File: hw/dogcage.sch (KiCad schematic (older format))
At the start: 17 parts, among them CON1 BARREL_JACK, M1 XBEE, P1 Door Sensor, P2 Servo, P3 CONN_01X10, P4 CONN_01X10, P5 CONN_01X14, P7 CONN_01X14, Q1 TIP120, SW1 SW_PUSH, U1 LD1117S33TR, U2 TEENSYLC

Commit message: Bulk cap to 5V and current limiting resistor to TIP120 base
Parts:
- added C3: 100uF, symbol C
- added R2: 470, symbol R
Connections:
- wire segments 89 -> 92
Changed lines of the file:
@@
 L +5V #PWR012
 U 1 1 553C62D3
-P 2950 1000
-F 0 "#PWR012" H 2950 850 50  0001 C CNN
-F 1 "+5V" H 2950 1140 50  0000 C CNN
-F 2 "" H 2950 1000 60  0000 C CNN
-F 3 "" H 2950 1000 60  0000 C CNN
-	1    2950 1000
+P 2850 1000
+F 0 "#PWR012" H 2850 850 50  0001 C CNN
+F 1 "+5V" H 2850 1140 50  0000 C CNN
+F 2 "" H 2850 1000 60  0000 C CNN
+F 3 "" H 2850 1000 60  0000 C CNN
+	1    2850 1000
 	1    0    0    -1
 $EndComp
@@
 	3250 1550 3250 1600
 Wire Wire Line
-	3250 1600 4450 1600
+	2900 1600 4450 1600
 Connection ~ 3850 1600
 Wire Wire Line
@@
 	2050 1150 2350 1150
 Wire Wire Line
-	2950 1000 2950 1150
-Wire Wire Line
-	2950 1150 3450 1150
+	2850 1000 2850 1150
+Wire Wire Line
+	2850 1150 3450 1150
 Wire Wire Line
 	3250 1250 3250 1150
@@
 	7850 3500 6850 3500
 Wire Wire Line
-	6850 3500 6850 4750
+	6850 3500 6850 4150
 Wire Wire Line
 	6850 4750 7150 4750
@@
 Text Label 8650 1600 0    60   ~ 0
 XBEE_CTL
+$Comp
+L R R2
+U 1 1 558214B8
+P 6850 4300
+F 0 "R2" V 6930 4300 50  0000 C CNN
+F 1 "470" V 6850 4300 50  0000 C CNN
+F 2 "" V 6780 4300 30  0000 C CNN
+F 3 "" H 6850 4300 30  0000 C CNN
+	1    6850 4300
+	1    0    0    -1
+$EndComp
+Wire Wire Line
+	6850 4750 6850 4450
+$Comp
+L C C3
+U 1 1 55821ABF
+P 2900 1400
+F 0 "C3" H 2925 1500 50  0000 L CNN
+F 1 "100uF" H 2925 1300 50  0000 L CNN
+F 2 "" H 2938 1250 30  0000 C CNN
+F 3 "" H 2900 1400 60  0000 C CNN
+	1    2900 1400
+	1    0    0    -1
+$EndComp
+Wire Wire Line
+	2900 1150 2900 1250
+Connection ~ 2900 1150
+Connection ~ 3250 1600
+Wire Wire Line
+	2900 1550 2900 1600
 $EndSCHEMATC

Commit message: Added lock servo
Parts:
- added P?: Lock, Pin_Headers:Pin_Header_Straight_1x03, symbol CONN_01X03
- added Q?: TIP120, ~, symbol TIP120
- added R?: 470, symbol R
- P2: value Servo -> Door
- Q1: footprint Power_Integrations:TO-220 -> ~
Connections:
- wire segments 92 -> 118
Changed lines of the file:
@@
 P 7950 4050
 F 0 "P2" H 7950 4250 50  0000 C CNN
-F 1 "Servo" V 8050 4050 50  0000 C CNN
+F 1 "Door" V 8050 4050 50  0000 C CNN
 F 2 "Pin_Headers:Pin_Header_Straight_1x03" H 7950 4050 60  0001 C CNN
 F 3 "" H 7950 4050 60  0000 C CNN
@@
 F 0 "Q1" H 7600 4825 50  0000 L CNN
 F 1 "TIP120" H 7600 4750 50  0000 L CNN
-F 2 "Power_Integrations:TO-220" H 7600 4675 50  0000 L CIN
+F 2 "~" H 7600 4675 50  0000 L CIN
 F 3 "" H 7350 4750 50  0000 L CNN
 	1    7350 4750
@@
 	7450 4150 7750 4150
 Wire Wire Line
-	4250 1150 4800 1150
+	4250 1150 4450 1150
+Wire Wire Line
+	4450 1150 4800 1150
 Wire Wire Line
 	4800 1150 4800 1000
 Wire Wire Line
-	3850 1450 3850 1700
+	3850 1450 3850 1600
+Wire Wire Line
+	3850 1600 3850 1700
 Wire Wire Line
 	3250 1550 3250 1600
 Wire Wire Line
-	2900 1600 4450 1600
+	2900 1600 3250 1600
+Wire Wire Line
+	3250 1600 3850 1600
+Wire Wire Line
+	3850 1600 4450 1600
 Connection ~ 3850 1600
 Wire Wire Line
@@
 	2850 1000 2850 1150
 Wire Wire Line
-	2850 1150 3450 1150
+	2850 1150 2900 1150
+Wire Wire Line
+	2900 1150 3250 1150
+Wire Wire Line
+	3250 1150 3450 1150
 Wire Wire Line
 	3250 1250 3250 1150
@@
 $EndComp
 Wire Wire Line
-	1500 2950 1950 2950
+	1500 2950 1750 2950
+Wire Wire Line
+	1750 2950 1950 2950
 Wire Wire Line
 	1500 3050 1950 3050
@@
 $EndComp
 Wire Wire Line
-	3750 3450 4300 3450
+	3750 3450 4000 3450
+Wire Wire Line
+	4000 3450 4300 3450
 Wire Wire Line
 	4000 3450 4000 4050
@@
 	6050 2400 6650 2400
 Wire Wire Line
-	6050 2600 6650 2600
-Wire Wire Line
-	6050 2500 6650 2500
+	6050 2600 6350 2600
+Wire Wire Line
+	6350 2600 6650 2600
+Wire Wire Line
+	6050 2500 6300 2500
+Wire Wire Line
+	6300 2500 6650 2500
 Wire Wire Line
 	6650 2300 6050 2300
@@
 	8650 2500 9100 2500
 Wire Wire Line
-	8650 2600 9100 2600
+	8650 2600 8850 2600
+Wire Wire Line
+	8850 2600 9100 2600
 Wire Wire Line
 	9100 2300 8650 2300
@@
 	8650 1400 9100 1400
 Wire Wire Line
-	8650 1300 9100 1300
+	8650 1300 8850 1300
+Wire Wire Line
+	8850 1300 9100 1300
 Connection ~ 8850 1300
 Wire Wire Line
 	5750 3800 5750 3650
 Wire Wire Line
-	7450 3100 7450 3950
-Wire Wire Line
-	1500 3850 1950 3850
+	7450 3100 7450 3700
+Wire Wire Line
+	7450 3700 7450 3950
+Wire Wire Line
+	1500 3850 1750 3850
+Wire Wire Line
+	1750 3850 1950 3850
 Wire Wire Line
 	1750 3850 1750 4050
 Connection ~ 1750 3850
 Wire Wire Line
-	6050 1300 6650 1300
+	6050 1300 6350 1300
+Wire Wire Line
+	6350 1300 6650 1300
 Wire Wire Line
 	6350 1300 6350 950
@@
 Wire Wire Line
 	2900 1550 2900 1600
+$Comp
+L TIP120 Q?
+U 1 1 559DEA4D
+P 9250 4750
+F 0 "Q?" H 9500 4825 50  0000 L CNN
+F 1 "TIP120" H 9500 4750 50  0000 L CNN
+F 2 "~" H 9500 4675 50  0000 L CIN
+F 3 "" H 9250 4750 50  0000 L CNN
+	1    9250 4750
+	1    0    0    -1
+$EndComp
+$Comp
+L CONN_01X03 P?
+U 1 1 559DEAB0
+P 10000 4050
+F 0 "P?" H 10000 4250 50  0000 C CNN
+F 1 "Lock" V 10100 4050 50  0000 C CNN
+F 2 "Pin_Headers:Pin_Header_Straight_1x03" H 10000 4050 60  0001 C CNN
+F 3 "" H 10000 4050 60  0000 C CNN
+	1    10000 4050
+	1    0    0    -1
+$EndComp
+Wire Wire Line
+	9800 4150 9350 4150
+Wire Wire Line
+	9350 4150 9350 4550
+Wire Wire Line
+	9800 3950 9350 3950
+Wire Wire Line
+	9350 3950 9350 3700
+Wire Wire Line
+	9350 3700 7450 3700
+Connection ~ 7450 3700
+$Comp
+L R R?
+U 1 1 559DEC4E
+P 8850 4300
+F 0 "R?" V 8930 4300 50  0000 C CNN
+F 1 "470" V 8850 4300 50  0000 C CNN
+F 2 "" V 8780 4300 30  0000 C CNN
+F 3 "" H 8850 4300 30  0000 C CNN
+	1    8850 4300
+	1    0    0    -1
+$EndComp
+Wire Wire Line
+	8850 4150 8850 2600
+Connection ~ 8850 2600
+Wire Wire Line
+	8850 4450 8850 4750
+Wire Wire Line
+	8850 4750 9050 4750
+$Comp
+L +5V #PWR?
+U 1 1 559DEDBC
+P 9100 3950
+F 0 "#PWR?" H 9100 3800 50  0001 C CNN
+F 1 "+5V" H 9100 4090 50  0000 C CNN
+F 2 "" H 9100 3950 60  0000 C CNN
+F 3 "" H 9100 3950 60  0000 C CNN
+	1    9100 3950
+	1    0    0    -1
+$EndComp
+Wire Wire Line
+	9100 3950 9100 4050
+Wire Wire Line
+	9100 4050 9800 4050
+$Comp
+L GND #PWR?
+U 1 1 559DEE7F
+P 9350 5150
+F 0 "#PWR?" H 9350 4900 50  0001 C CNN
+F 1 "GND" H 9350 5000 50  0000 C CNN
+F 2 "" H 9350 5150 60  0000 C CNN
+F 3 "" H 9350 5150 60  0000 C CNN
+	1    9350 5150
+	1    0    0    -1
+$EndComp
+Wire Wire Line
+	9350 5150 9350 4950
 $EndSCHEMATC

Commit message: Added 5V regulator to schematic
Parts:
- added C1: 10uF, Capacitors_Elko_ThroughHole:Elko_vert_11x5mm_RM2, symbol CP
- added C4: 100uF, Capacitors_Elko_ThroughHole:Elko_vert_11x5mm_RM2, symbol CP
- added U1: LD1117S50TR, SOT-223, symbol LD1117S50TR
- C3: value 100uF -> .1uF
- U2: renamed from U1; footprint SMD_Packages:SOT-223 -> SOT-223
- gave numbers to parts that had none: 3
- renumbered C1 to C2, C2 to C5, D2 to D1, D1 to D2, P3 to P1, P4 to P2, P5 to P3, P1 to P4, P2 to P5, P7 to P6, U2 to U3
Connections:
- net labels added: VCC
- wire segments 118 -> 109
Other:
- moved on the sheet: C2, C5, D2, R1, U2

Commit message: Removed XBee, moved bulk cap to be close to servo
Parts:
- removed C3: .1uF, symbol C
- removed M1: XBEE, modules:xbee, symbol XBEE
- removed P1, P2: CONN_01X10, Pin_Headers:Pin_Header_Straight_1x10, symbol CONN_01X10
- added 10K (x3): R, symbol R
- added SW?: SW_PUSH, symbol SW_PUSH
- added U?: ESP-01v090, symbol ESP-01v090
- C1: value 10uF -> .1uF
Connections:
- wire segments 109 -> 122
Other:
- moved on the sheet: C2, C4, C5, D2, P4, R1, R2, SW1, U2

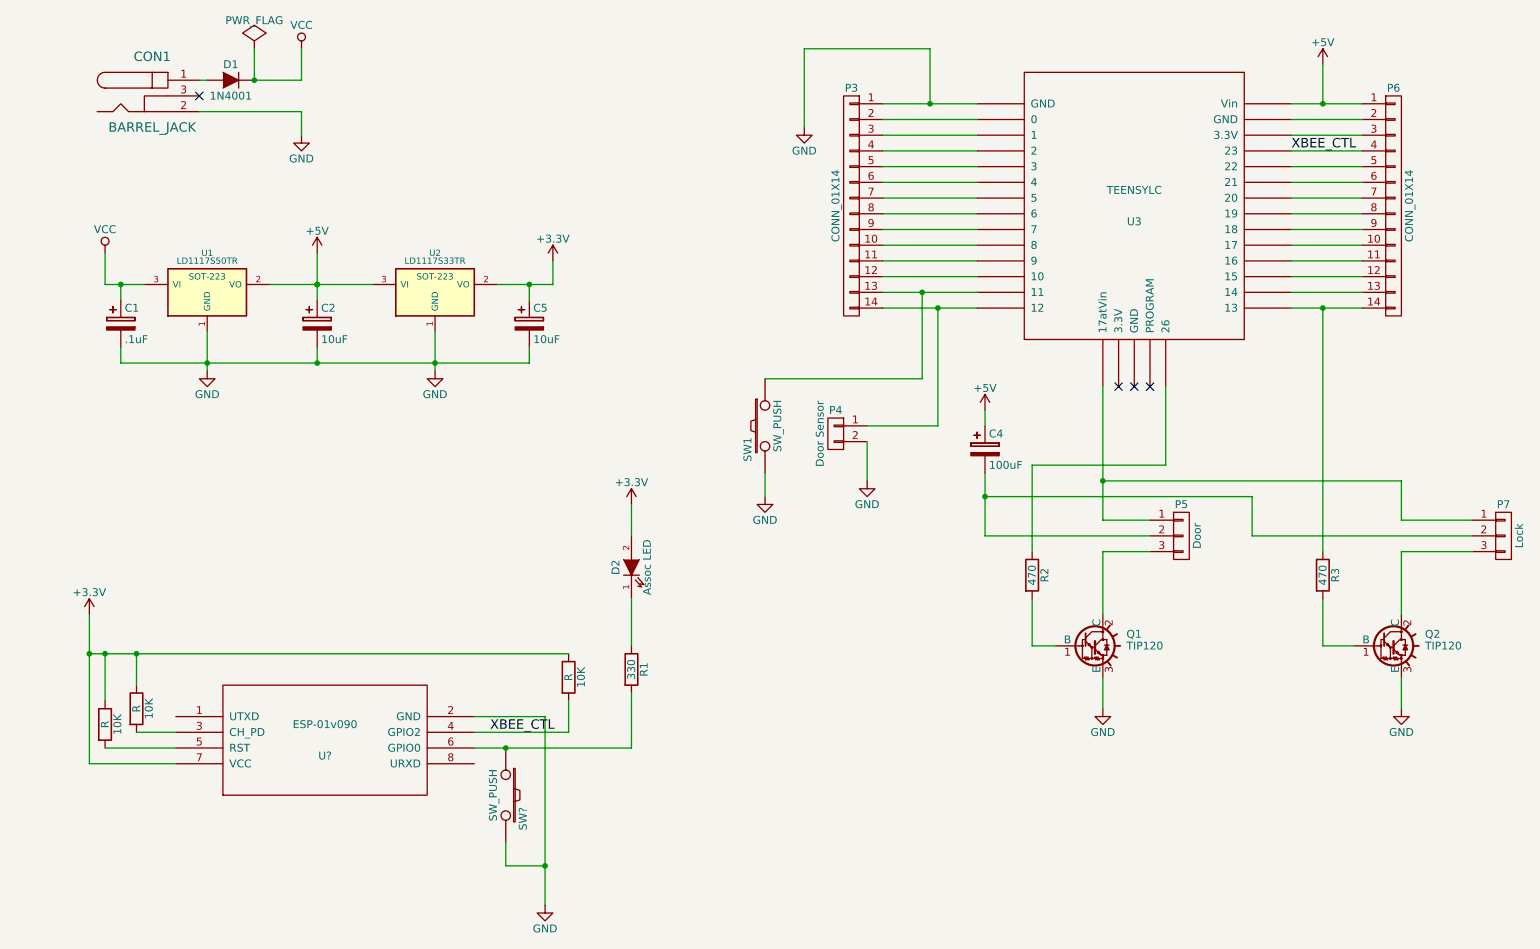
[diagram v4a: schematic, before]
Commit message: Removed Teensy breakout, still wiring up
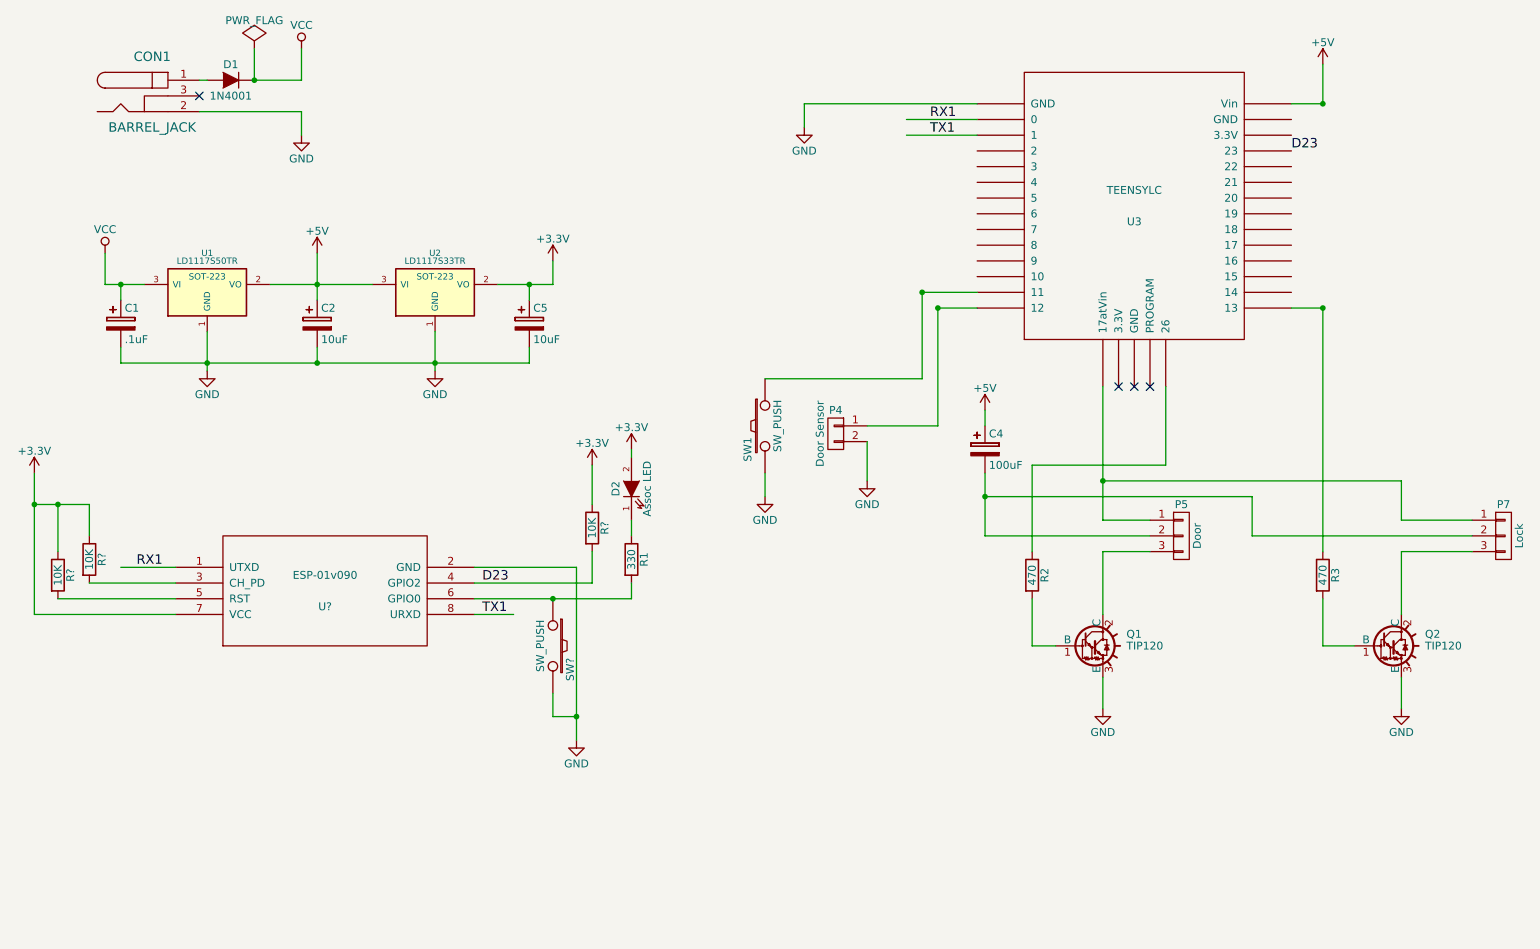
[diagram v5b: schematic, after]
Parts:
- removed 10K (x3): R, symbol R
- removed P3, P6: CONN_01X14, Pin_Headers:Pin_Header_Straight_1x14, symbol CONN_01X14
- added R? (x3): 10K, symbol R
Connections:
- net labels added: D23, RX1, TX1
- net labels removed: XBEE_CTL
- wire segments 122 -> 95
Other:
- moved on the sheet: D2, R1, SW?, U?

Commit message: Removed door sensor
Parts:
- removed P4: Door Sensor, Pin_Headers:Pin_Header_Straight_1x02, symbol CONN_01X02
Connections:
- wire segments 95 -> 91
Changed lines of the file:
@@
-$EndComp
-$Comp
-L CONN_01X02 P4
-U 1 1 553C4802
-P 5750 3400
-F 0 "P4" H 5750 3550 50  0000 C CNN
-F 1 "Door Sensor" V 5850 3400 50  0000 C CNN
-F 2 "Pin_Headers:Pin_Header_Straight_1x02" H 5750 3400 60  0001 C CNN
-F 3 "" H 5750 3400 60  0000 C CNN
-	1    5750 3400
-	-1   0    0    -1
-$EndComp
-$Comp
-L GND #PWR13
-U 1 1 553C48BE
-P 5950 3700
-F 0 "#PWR13" H 5950 3450 50  0001 C CNN
-F 1 "GND" H 5950 3550 50  0000 C CNN
-F 2 "" H 5950 3700 60  0000 C CNN
-F 3 "" H 5950 3700 60  0000 C CNN
-	1    5950 3700
-	-1   0    0    -1
 $EndComp
 $Comp
@@
 	8850 1050 8850 1300
 Wire Wire Line
-	5950 3450 5950 3700
-Wire Wire Line
 	1700 1150 1750 1150
 Wire Wire Line
@@
 	8400 3800 6700 3800
 Connection ~ 6700 3800
-Wire Wire Line
-	6400 2600 6650 2600
-Wire Wire Line
-	5950 3350 6400 3350
-Wire Wire Line
-	6400 3350 6400 2600
-Connection ~ 6400 2600
 Connection ~ 2450 2950
 Wire Wire Line

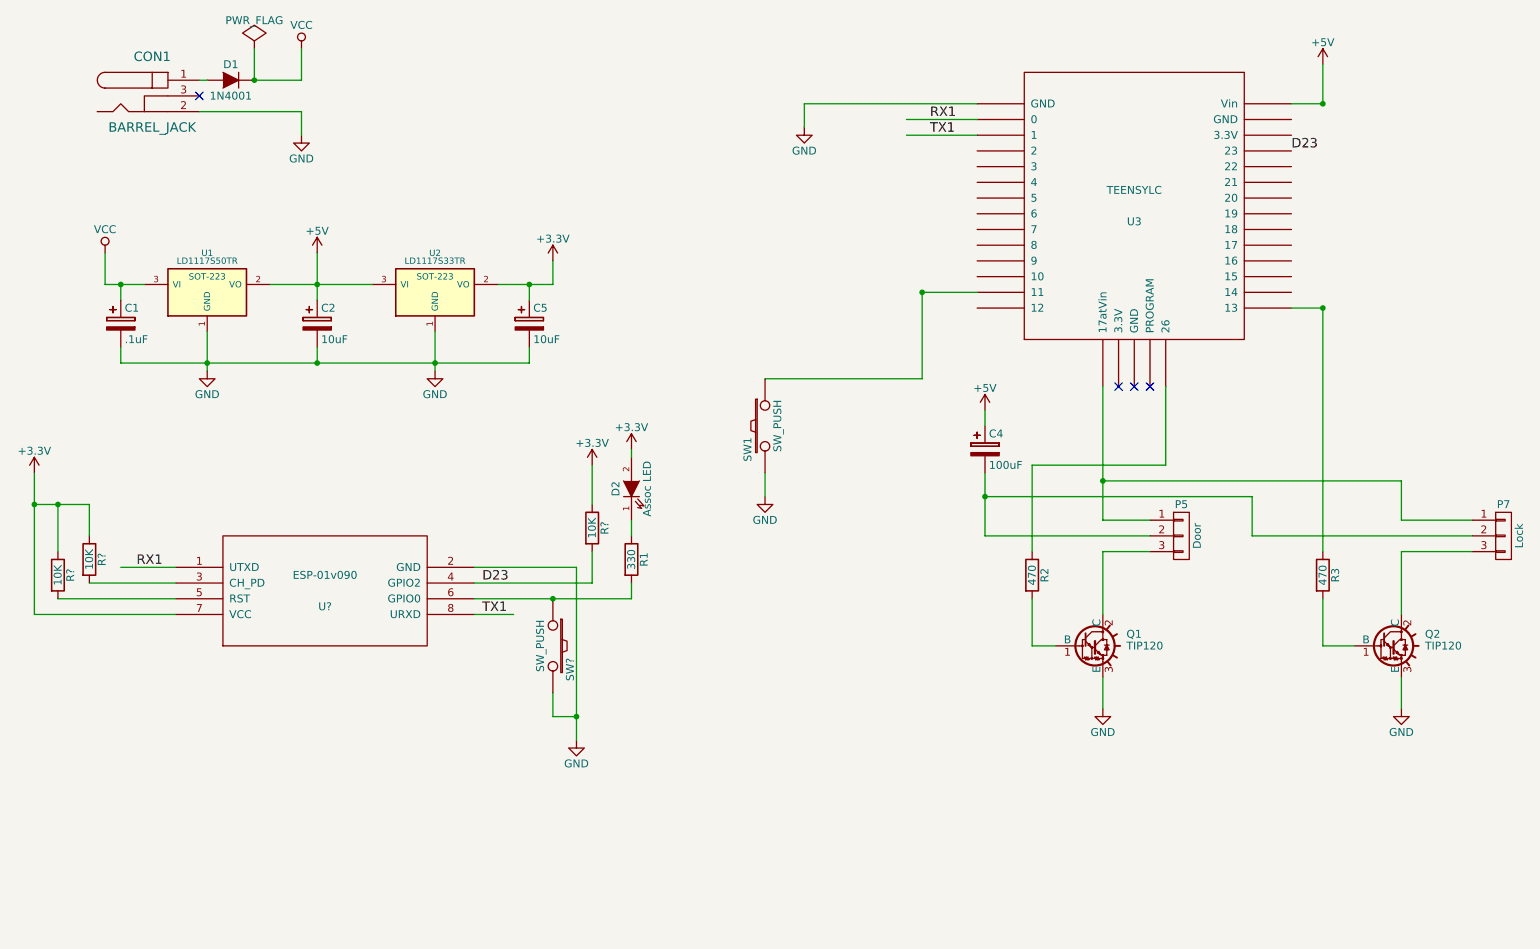
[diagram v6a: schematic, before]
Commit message: Cleaned up Teensy connections, still getting DRC errors
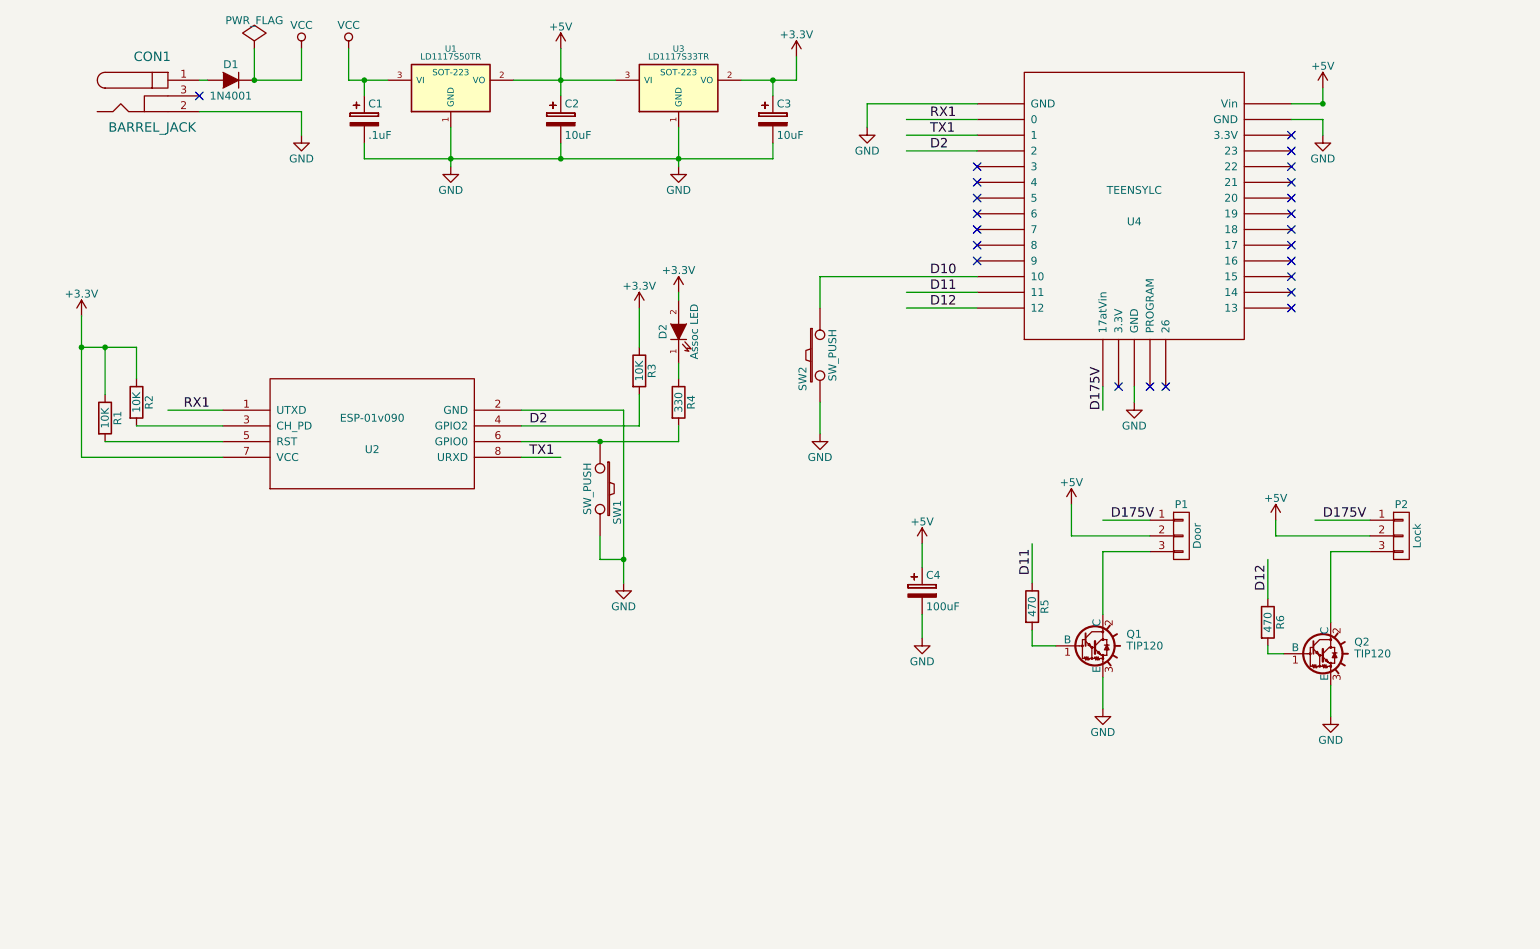
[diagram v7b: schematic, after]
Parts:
- gave numbers to parts that had none: 5
- renumbered C5 to C3, P5 to P1, P7 to P2, R1 to R4, R2 to R5, R3 to R6, SW1 to SW2, U2 to U3, U3 to U4
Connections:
- net labels added: D10, D11, D12, D175V, D2
- net labels removed: D23
- wire segments 91 -> 76
- no-connect marks 4 -> 23
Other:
- moved on the sheet: C1, C2, C3, C4, D2, P2, Q2, R1, R2, R3, R4, R5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
